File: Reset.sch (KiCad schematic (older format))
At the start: 12 parts, among them U1 74HCU04, U5 74HC00, U6 74HC04, U7 74HC05

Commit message: route part of A8-A15 from WKL to WKH
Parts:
- R4, R5, R6, R7: footprint Resistor_THT:R_Axial_DIN0207_L6.3mm_D2.5mm_P10.16mm_Horizontal -> Resistor_THT:R_Axial_DIN0204_L3.6mm_D1.6mm_P5.08mm_Horizontal
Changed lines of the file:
@@
 F 0 "R4" H 1420 4196 50  0000 L CNN
 F 1 "10k" H 1420 4105 50  0000 L CNN
-F 2 "Resistor_THT:R_Axial_DIN0207_L6.3mm_D2.5mm_P10.16mm_Horizontal" V 1280 4150 50  0001 C CNN
+F 2 "Resistor_THT:R_Axial_DIN0204_L3.6mm_D1.6mm_P5.08mm_Horizontal" V 1280 4150 50  0001 C CNN
 F 3 "~" H 1350 4150 50  0001 C CNN
 	1    1350 4150
@@
 F 0 "R5" V 2457 4400 50  0000 C CNN
 F 1 "10k" V 2366 4400 50  0000 C CNN
-F 2 "Resistor_THT:R_Axial_DIN0207_L6.3mm_D2.5mm_P10.16mm_Horizontal" V 2180 4400 50  0001 C CNN
+F 2 "Resistor_THT:R_Axial_DIN0204_L3.6mm_D1.6mm_P5.08mm_Horizontal" V 2180 4400 50  0001 C CNN
 F 3 "~" H 2250 4400 50  0001 C CNN
 	1    2250 4400
@@
 F 0 "R6" V 3357 3750 50  0000 C CNN
 F 1 "100k" V 3266 3750 50  0000 C CNN
-F 2 "Resistor_THT:R_Axial_DIN0207_L6.3mm_D2.5mm_P10.16mm_Horizontal" V 3080 3750 50  0001 C CNN
+F 2 "Resistor_THT:R_Axial_DIN0204_L3.6mm_D1.6mm_P5.08mm_Horizontal" V 3080 3750 50  0001 C CNN
 F 3 "~" H 3150 3750 50  0001 C CNN
 	1    3150 3750
@@
 F 0 "R7" H 4420 2946 50  0000 L CNN
 F 1 "10k" H 4420 2855 50  0000 L CNN
-F 2 "Resistor_THT:R_Axial_DIN0207_L6.3mm_D2.5mm_P10.16mm_Horizontal" V 4280 2900 50  0001 C CNN
+F 2 "Resistor_THT:R_Axial_DIN0204_L3.6mm_D1.6mm_P5.08mm_Horizontal" V 4280 2900 50  0001 C CNN
 F 3 "~" H 4350 2900 50  0001 C CNN
 	1    4350 2900

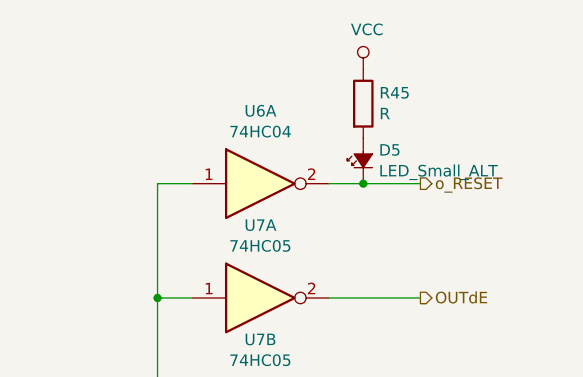
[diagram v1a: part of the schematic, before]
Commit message: route the iBn bus on the left side of the board
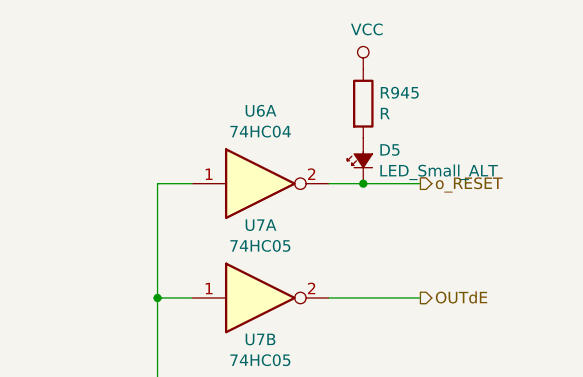
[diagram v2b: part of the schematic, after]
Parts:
- renumbered R45 to R945
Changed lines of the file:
@@
 	6250 2000 6100 2000
 $Comp
-L Device:R R45
+L Device:R R945
 U 1 1 63473D7C
 P 6250 1650
-F 0 "R45" H 6320 1696 50  0000 L CNN
+F 0 "R945" H 6320 1696 50  0000 L CNN
 F 1 "R" H 6320 1605 50  0000 L CNN
 F 2 "Resistor_THT:R_Axial_DIN0207_L6.3mm_D2.5mm_P10.16mm_Horizontal" V 6180 1650 50  0001 C CNN
